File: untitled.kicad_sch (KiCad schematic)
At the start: 0 parts

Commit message: VGA design
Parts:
- added J1: ~, symbol PMod:PMod j1
- added J2: ~, symbol PMod:PMod_j2
- added R10, R11, R12, R13, R14, R15, R16, R17, R18, R19, R20, R21, R22, R23: 100K, symbol Device:R
- added U3, U4: SN74ALVC245PWR, PW20, symbol 2025-09-12_09-11-34:SN74ALVC245PWR
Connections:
- net GND: now also R10.2, R11.2, R12.2, R13.2, R14.2, R15.2, R16.2, R17.2, R18.2, R19.2, R20.2, R21.2, R22.2, R23.2, U3.10 (GND), U3.19 (*OE), U4.10 (GND), U4.19 (*OE)
- new net: J1.7 (B0), R10.1, U3.6 (A5)
- new net: J2.2 (G1), R21.1, U4.7 (A6)
- new net: J1.1 (R0), R14.1, U3.2 (A1)
- new net: J1.10 (B3), R11.1, U3.9 (A8)
- new net: J1.2 (R1), R15.1, U3.3 (A2)
- new net: J1.3 (R2), R16.1, U3.4 (A3)
- new net: J1.4 (R3), R17.1, U3.5 (A4)
- new net: J1.8 (B1), R13.1, U3.7 (A6)
- new net: J1.9 (B2), R12.1, U3.8 (A7)
- new net: J2.3 (G2), R22.1, U4.8 (A7)
- new net: J2.8 (VS), R18.1, U4.4 (A3)
- new net: J2.4 (G3), R23.1, U4.9 (A8)
- new net: J2.1 (G0), R20.1, U4.6 (A5)
- new net: J2.7 (HS), R19.1, U4.5 (A4)
- new net +3.3V: U3.1 (DIR), U3.20 (VCC), U4.1 (DIR), U4.20 (VCC)
- no-connect marks 0 -> 2
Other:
- note added: "VGA_B0 VGA_B1 VGA_B2 VGA_B3"
- note added: "VGA_R0 VGA_R1 VGA_R2 VGA_R3"
- note added: "VGA_VS VGA_HS"

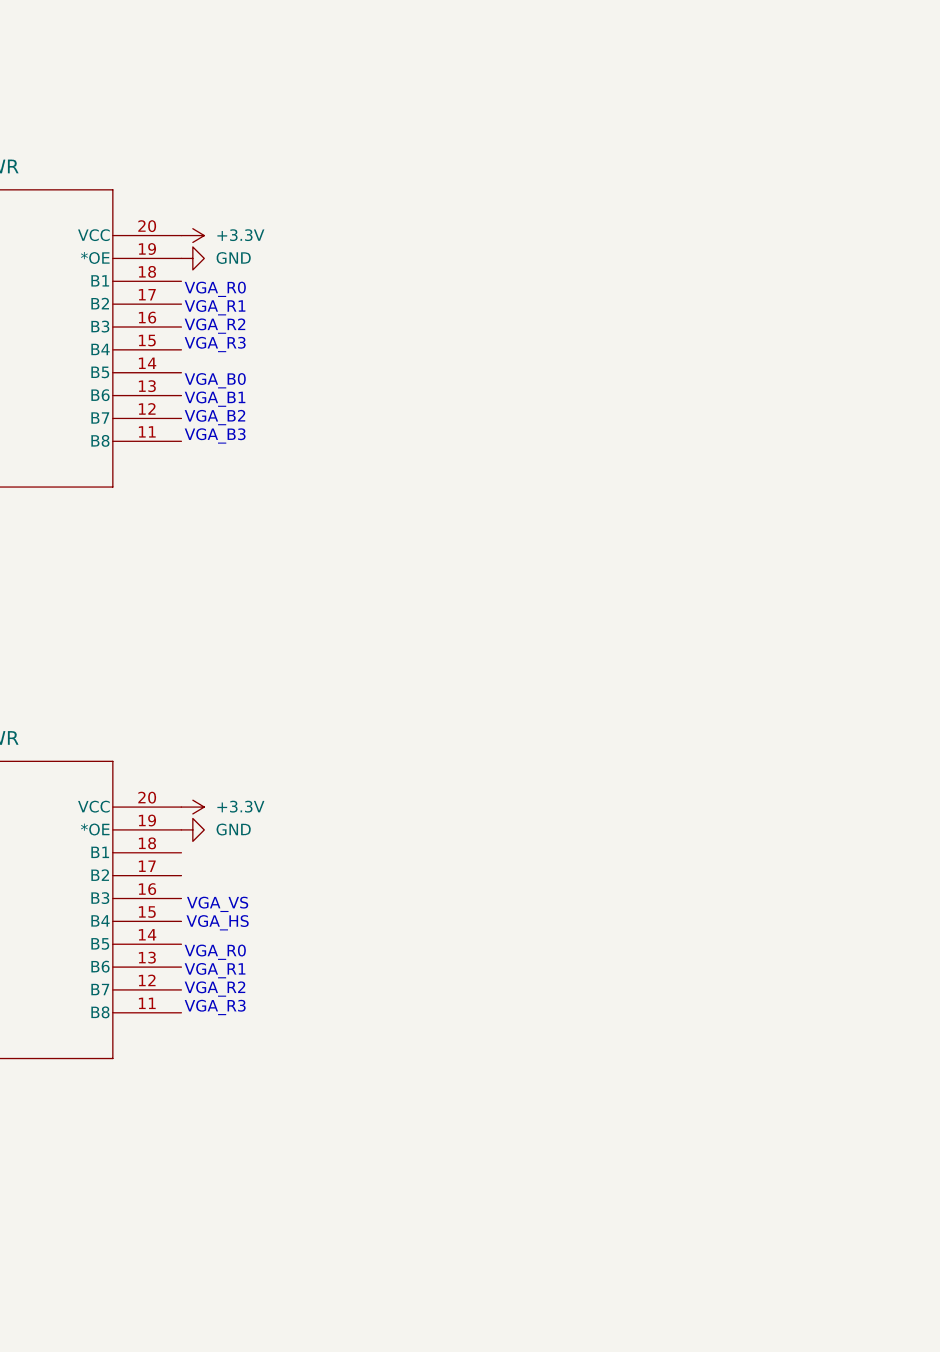
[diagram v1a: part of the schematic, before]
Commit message: link fpga to root
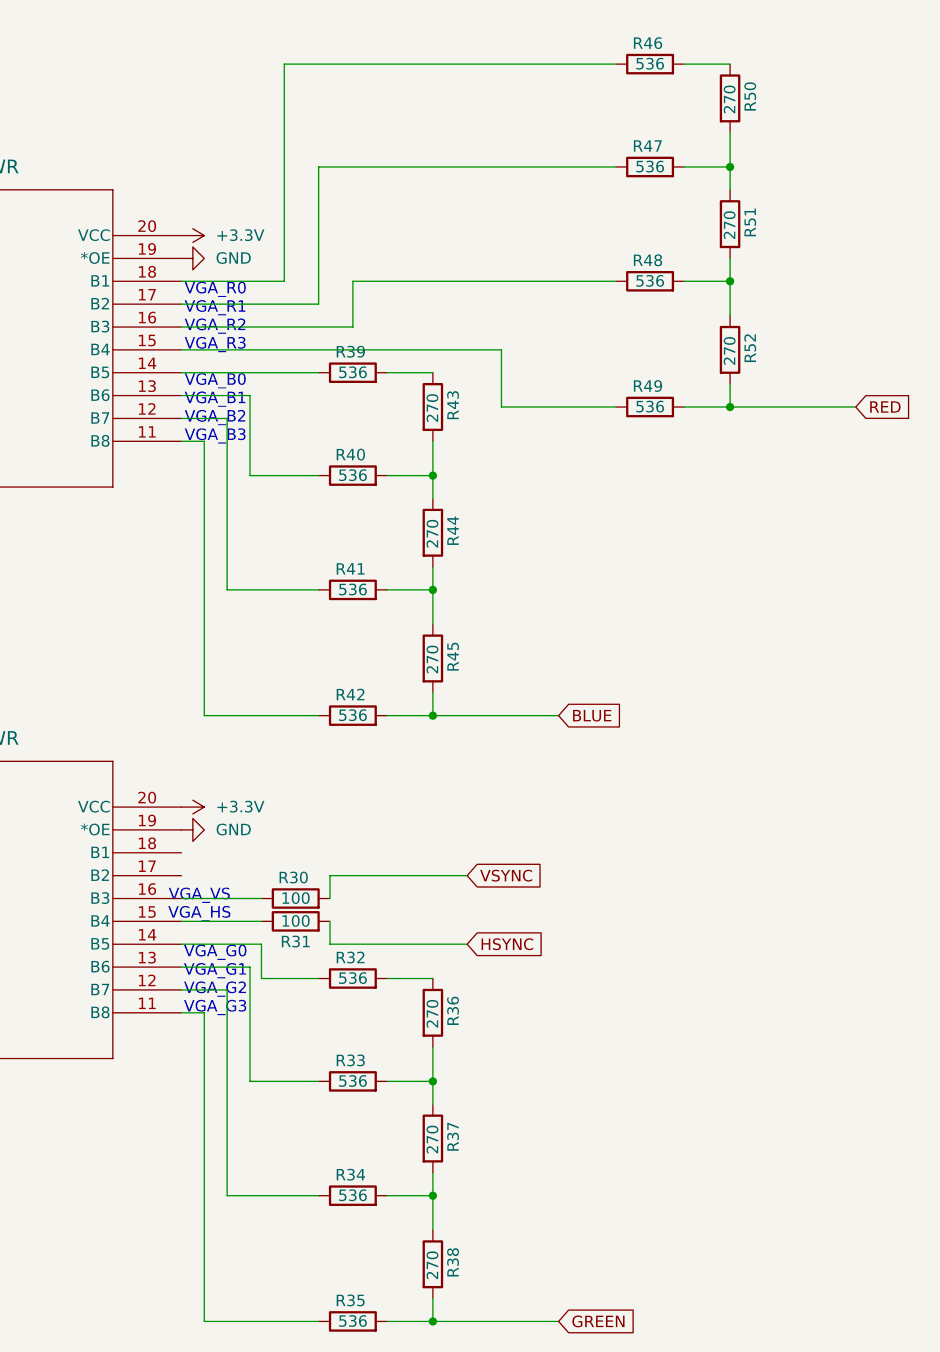
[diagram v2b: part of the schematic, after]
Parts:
- added R30, R31: 100, symbol Device:R
- added R32, R33, R34, R35, R39, R40, R41, R42, R46, R47, R48, R49: 536, symbol Device:R
- added R36, R37, R38, R43, R44, R45, R50, R51, R52: 270, symbol Device:R
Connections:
- net at U3.11 (B8): now also R42.1
- net at U3.12 (B7): now also R41.1
- net at U3.13 (B6): now also R40.1
- net at U3.14 (B5): now also R39.1
- net at U3.15 (B4): now also R49.1
- net at U3.16 (B3): now also R48.1
- net at U3.17 (B2): now also R47.1
- net at U3.18 (B1): now also R46.1
- net at U4.11 (B8): now also R35.1
- net at U4.12 (B7): now also R34.1
- net at U4.13 (B6): now also R33.1
- net at U4.14 (B5): now also R32.1
- net at U4.15 (B4): now also R31.1
- net at U4.16 (B3): now also R30.1
- new net: R46.2, R50.1
- new net: R48.2, R51.2, R52.1
- new net: R40.2, R43.2, R44.1
- new net: R41.2, R44.2, R45.1
- new net: R34.2, R37.2, R38.1
- new net: R32.2, R36.1
- new net: R33.2, R36.2, R37.1
- new net: R47.2, R50.2, R51.1
- new net: R39.2, R43.1
- new net BLUE: R42.2, R45.2
- new net GREEN: R35.2, R38.2
- new net HSYNC: R31.2
- new net RED: R49.2, R52.2
- new net VSYNC: R30.2
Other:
- note added: "VGA_G0 VGA_G1 VGA_G2 VGA_G3"

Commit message: link fpga
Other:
- note added: "Mangler å lage en connector"
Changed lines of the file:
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@@
+		)
+	)
+	(text "Mangler å lage en connector\n"
+		(exclude_from_sim no)
+		(at 248.412 97.536 0)
+		(effects
+			(font
+				(size 1.27 1.27)
+			)
 		)
 	)

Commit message: schematic for stm32u545
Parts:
- renumbered R11 to R10, R12 to R11, R13 to R12, R10 to R13, R30 to R24, R31 to R25, R39 to R26, R40 to R27, R41 to R28, R42 to R29, R32 to R30, R33 to R31, R34 to R32, R35 to R33, R43 to R34, R44 to R35, R45 to R36, R36 to R37, R37 to R38, R38 to R39, R46 to R40, R47 to R41, R48 to R42, R49 to R43, R50 to R44, R51 to R45, R52 to R46
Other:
- title: (none) -> 4bit_vga_out
